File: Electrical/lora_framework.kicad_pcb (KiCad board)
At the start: 4 copper layers, 26 x 30 mm, 22 parts, among them J1 Conn_Coaxial_Small, P1 USB_C_Plug_USB2.0, SW1 SW_Push, SW2 SW_Push, U1 E22-400MM22S, U2 STM32F042F6Px, U3 TLV76733DRVR

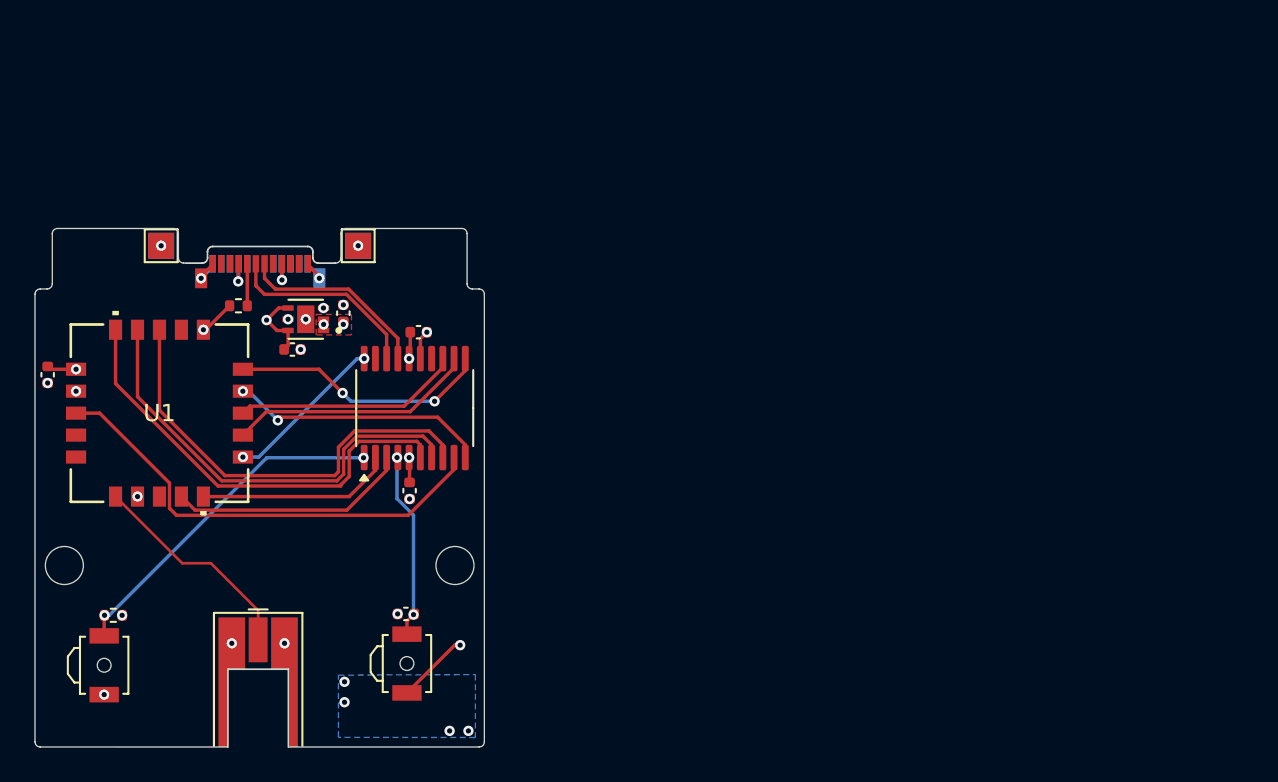
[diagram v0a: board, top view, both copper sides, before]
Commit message: swapped USB connector for easier assemb
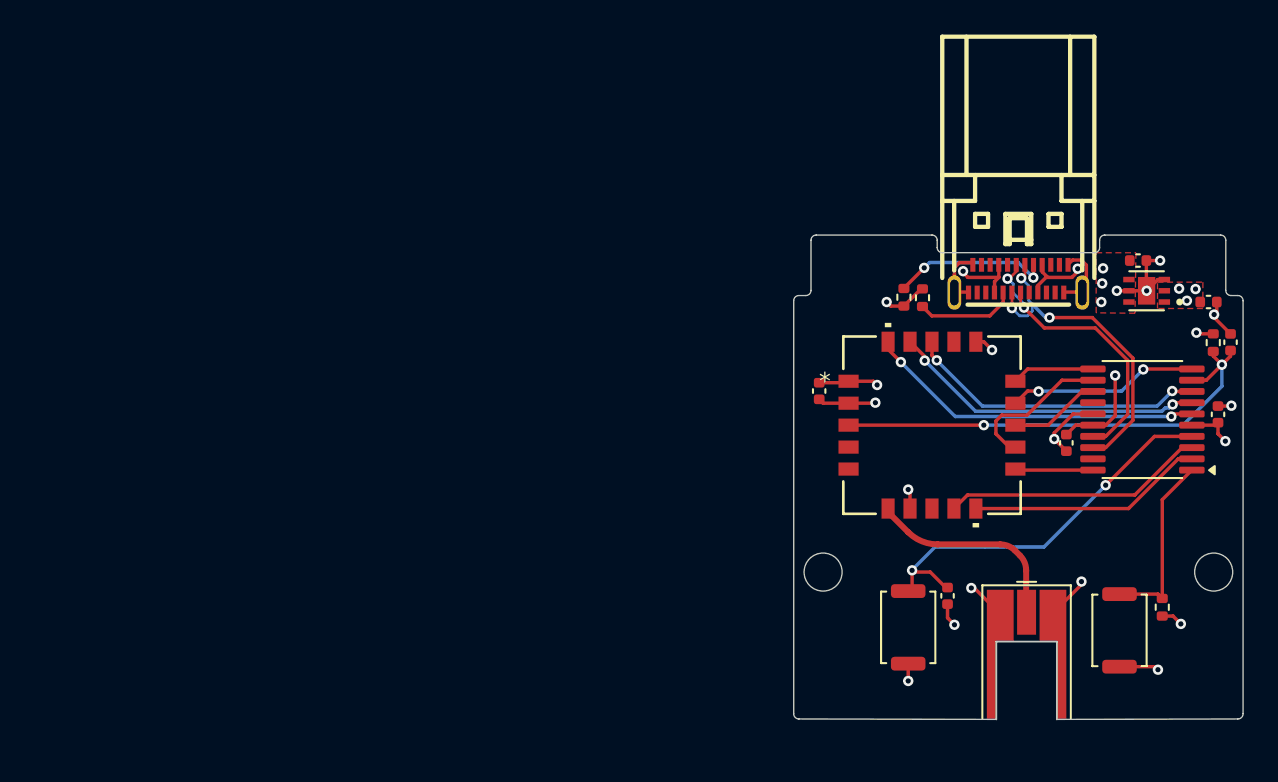
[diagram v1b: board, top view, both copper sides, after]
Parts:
- removed G***: LOGO, LOGO
- removed P1: USB_C_Plug_USB2.0, Connector_USB:USB_C_Plug_Molex_105444
- removed TP1, TP2, TP3, TP4: TestPoint, TestPoint:TestPoint_Pad_1.5x1.5mm
- added C7: 0.1nF, Capacitor_SMD:C_0402_1005Metric, F.Cu at (127.4, 28.3)
- added R3: 100k, Resistor_SMD:R_0402_1005Metric, F.Cu at (126.4, 28.3)
- added R4: 5.1k, Resistor_SMD:R_0402_1005Metric, F.Cu at (108.5, 25.7)
- added USB1: XDBM-0339-1530, footprints:USB-C-SMD_USB-3.1-C-TYPE, F.Cu at (115.1, 24.6)
- SW1, SW2: footprint Button_Switch_SMD:SW_SPST_B3U-3000P-B -> Button_Switch_SMD:SW_Push_SPST_NO_Alps_SKRK
- moved R2 60.7 mm to (123.5, 43.6), turned to -90 degrees
- moved SW1 58.8 mm to (121.0, 45.0)
- moved C5 50.1 mm to (126.2, 26.0), turned to 0 degrees
- moved C6 49.2 mm to (122.1, 23.6)
- moved U3 48.7 mm to (122.6, 25.3)
- moved C2 47.0 mm to (126.7, 32.5), turned to 90 degrees
- moved U1 44.7 mm to (110.2, 33.1)
- moved C4 44.7 mm to (103.6, 31.1)
- moved J1 44.5 mm to (115.6, 46.4)
- moved H1 43.9 mm to (103.8, 41.6)
- moved H2 43.9 mm to (126.5, 41.6)
- moved U2 42.1 mm to (122.3, 32.8), turned to 180 degrees
- moved R1 39.6 mm to (109.6, 25.7), turned to 90 degrees
- moved C1 38.0 mm to (117.9, 34.1), turned to -90 degrees
- moved C3 31.4 mm to (111.0, 43.0), turned to -90 degrees
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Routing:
- net GND: track 8.13 -> 35.8 mm, vias 23 -> 14
- net NRST: track 10.8 -> 23.2 mm
- net SPI1_SCK: track 15.1 -> 4.78 mm, vias 2 -> 0
- net Net-(USB1-CC2): track 0.00 -> 9.25 mm, vias 0 -> 2
- net BOOT0: track 20.0 -> 10.7 mm, vias 2 -> 0
- net DIO3: track 25.6 -> 17.4 mm, vias 0 -> 2
- net SPI1_MOSI: track 13.2 -> 5.29 mm
- net USB_DP: track 11.4 -> 19.3 mm, vias 0 -> 3
- net DIO2: track 25.8 -> 18.3 mm, vias 0 -> 2
- net +3.3V: track 8.94 -> 16.2 mm, vias 7 -> 9
- net DIO1: track 26.0 -> 19.7 mm, vias 0 -> 2
- net USB_DM: track 11.2 -> 17.1 mm, vias 0 -> 2
- net SPI1_MISO: track 14.4 -> 8.78 mm
- net BUSY: track 9.38 -> 4.51 mm, vias 2 -> 0
- net SPI1_NSS: track 15.0 -> 11.0 mm
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- added copper zone on F.Cu, net VBUS
- removed copper zone on B.Cu, net GND
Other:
- board size 26 x 30 mm -> 26 x 28 mm
- board text removed: "Designed by Madhav Kapa"
- board text removed: "Project Horizon"
